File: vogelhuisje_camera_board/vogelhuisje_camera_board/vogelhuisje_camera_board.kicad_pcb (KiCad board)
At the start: 2 copper layers, 39.4 x 95.2 mm, 20 parts, among them J1 Conn_01x21_Female, J4 Camera Connector, Q2 Q_NMOS_DGS

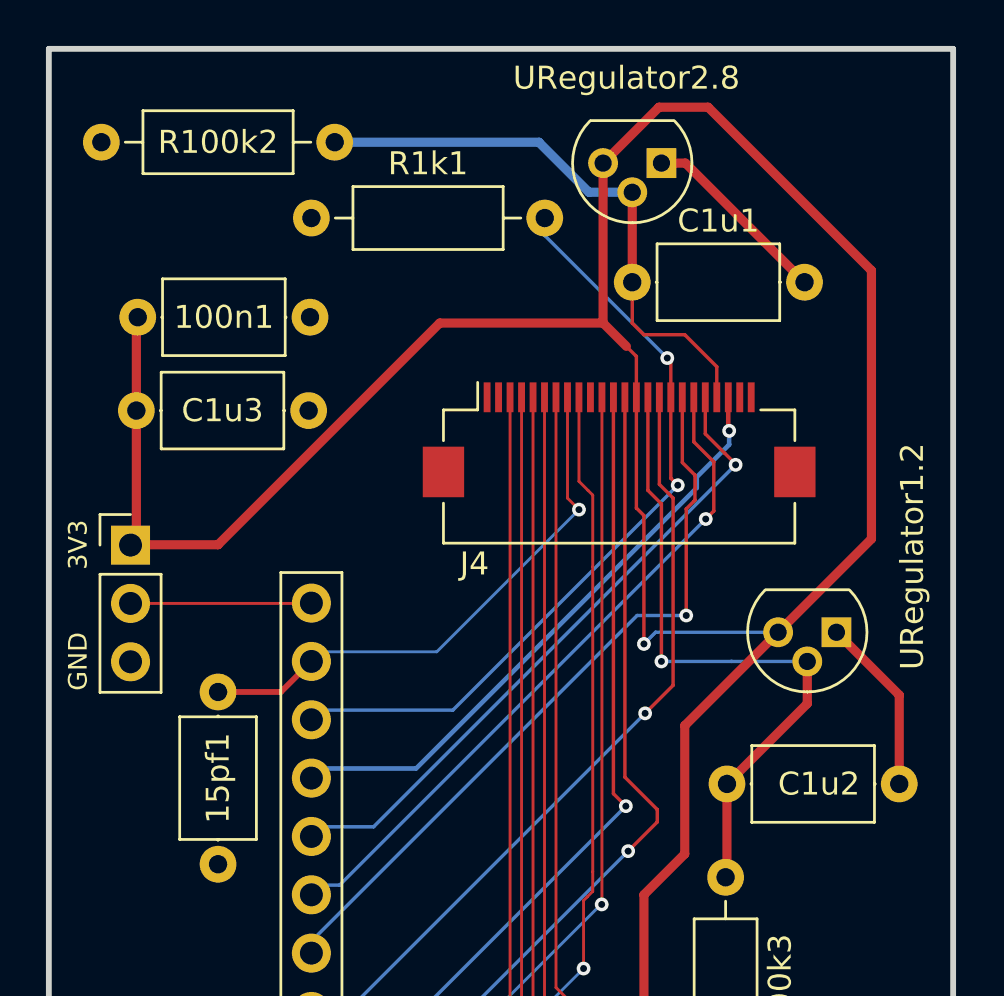
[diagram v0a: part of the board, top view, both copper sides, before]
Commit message: changed camera connector, and updated regulator pins
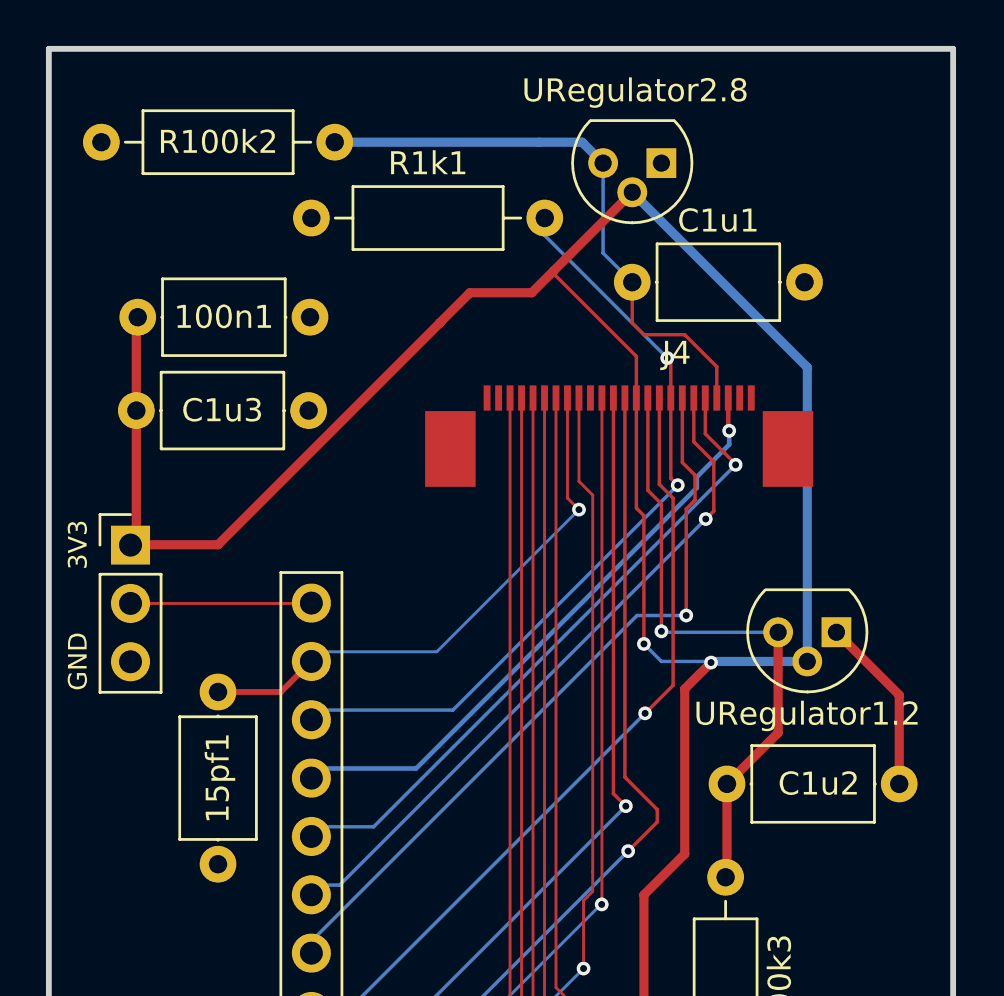
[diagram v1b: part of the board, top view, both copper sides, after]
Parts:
- J4: footprint Connector_FFC-FPC:Hirose_FH12-24S-0.5SH_1x24-1MP_P0.50mm_Horizontal -> components:camera_connector
- moved J4 2.50 mm to (117.5, 72.8)
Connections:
- URegulator1.2 pad 2: CSI_1.2V -> 3V3
- URegulator1.2 pad 3: 3V3 -> CSI_1.2V
- URegulator2.8 pad 2: CSI_2.8V -> 3V3
- URegulator2.8 pad 3: 3V3 -> CSI_2.8V
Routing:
- net 3V3: track 150.8 -> 139.7 mm, vias 1 -> 2
- net GND: track 16.1 -> 7.74 mm
- net CSI_1.2V: track 28.9 -> 27.1 mm

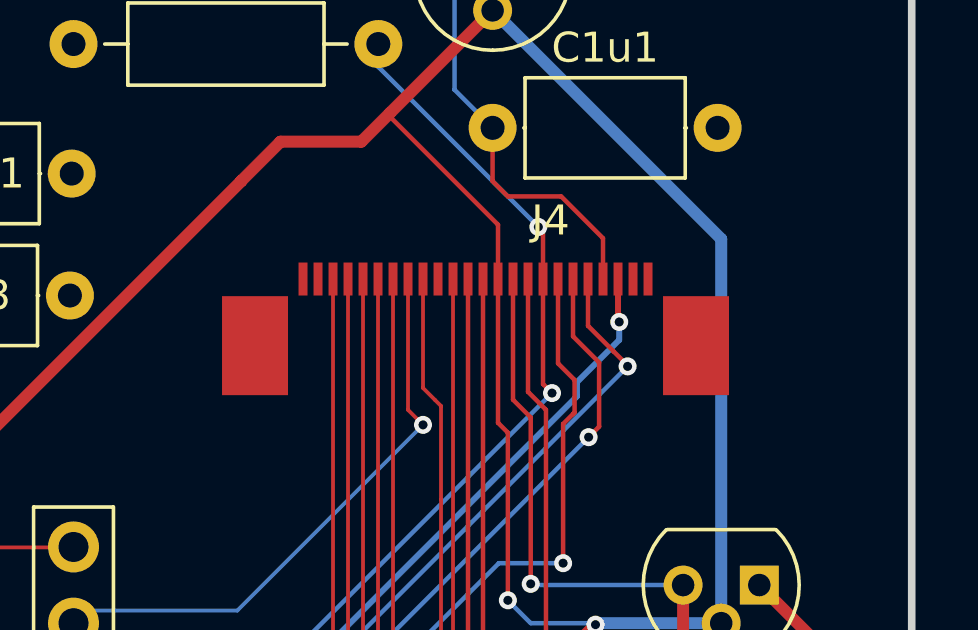
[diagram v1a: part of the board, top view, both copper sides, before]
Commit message: updated to use new connector footprint
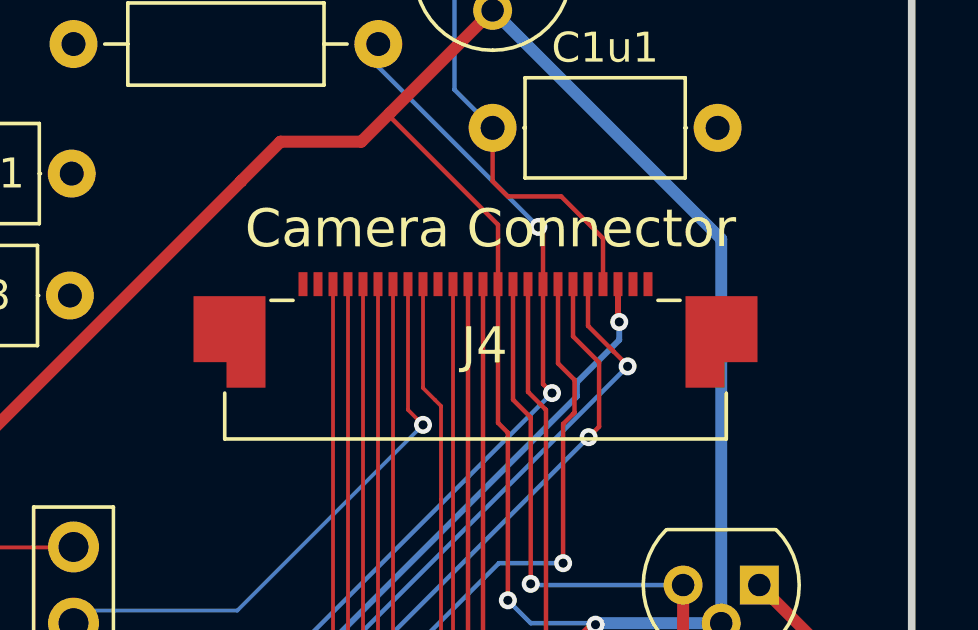
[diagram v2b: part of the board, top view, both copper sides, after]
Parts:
- J4: footprint components:camera_connector -> components:CONN_MOLEX_52437-2471
- moved J4 2.80 mm to (115.0, 74.1)
